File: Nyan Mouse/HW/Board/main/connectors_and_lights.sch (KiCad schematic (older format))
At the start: 49 parts, among them Q301 MOSFET-NCHANNELSMD, Q302 MOSFET-NCHANNELSMD, Q303 MOSFET-PCHANNELSMD, Q304 MOSFET-NCHANNELSMD, Q305 MOSFET-PCHANNELSMD, Q306 MOSFET-NCHANNELSMD, Q307 MOSFET-PCHANNELSMD, Q308 MOSFET-NCHANNELSMD, Q309 MOSFET-NCHANNELSMD, Q310 MOSFET-NCHANNELSMD, Q311 MOSFET-NCHANNELSMD, Q312 MOSFET-NCHANNELSMD, U301 74HC595, U302 74HC595, U303 74HC595

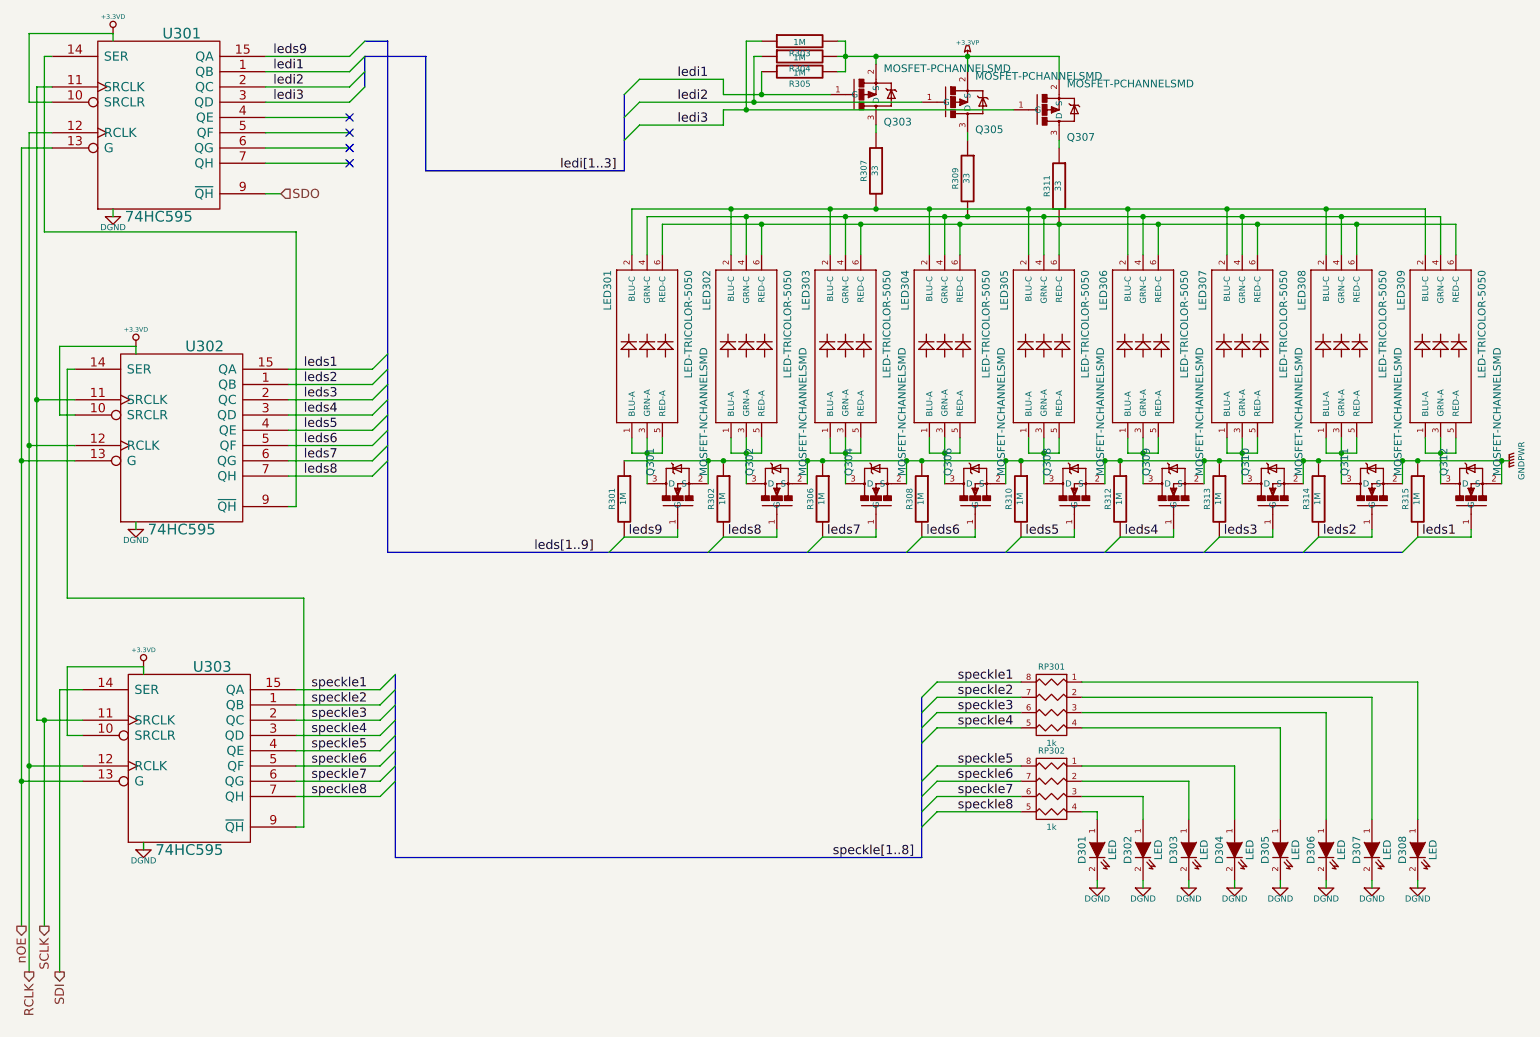
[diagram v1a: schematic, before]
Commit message: Flipped some RGB leds, added emitter pulldowns
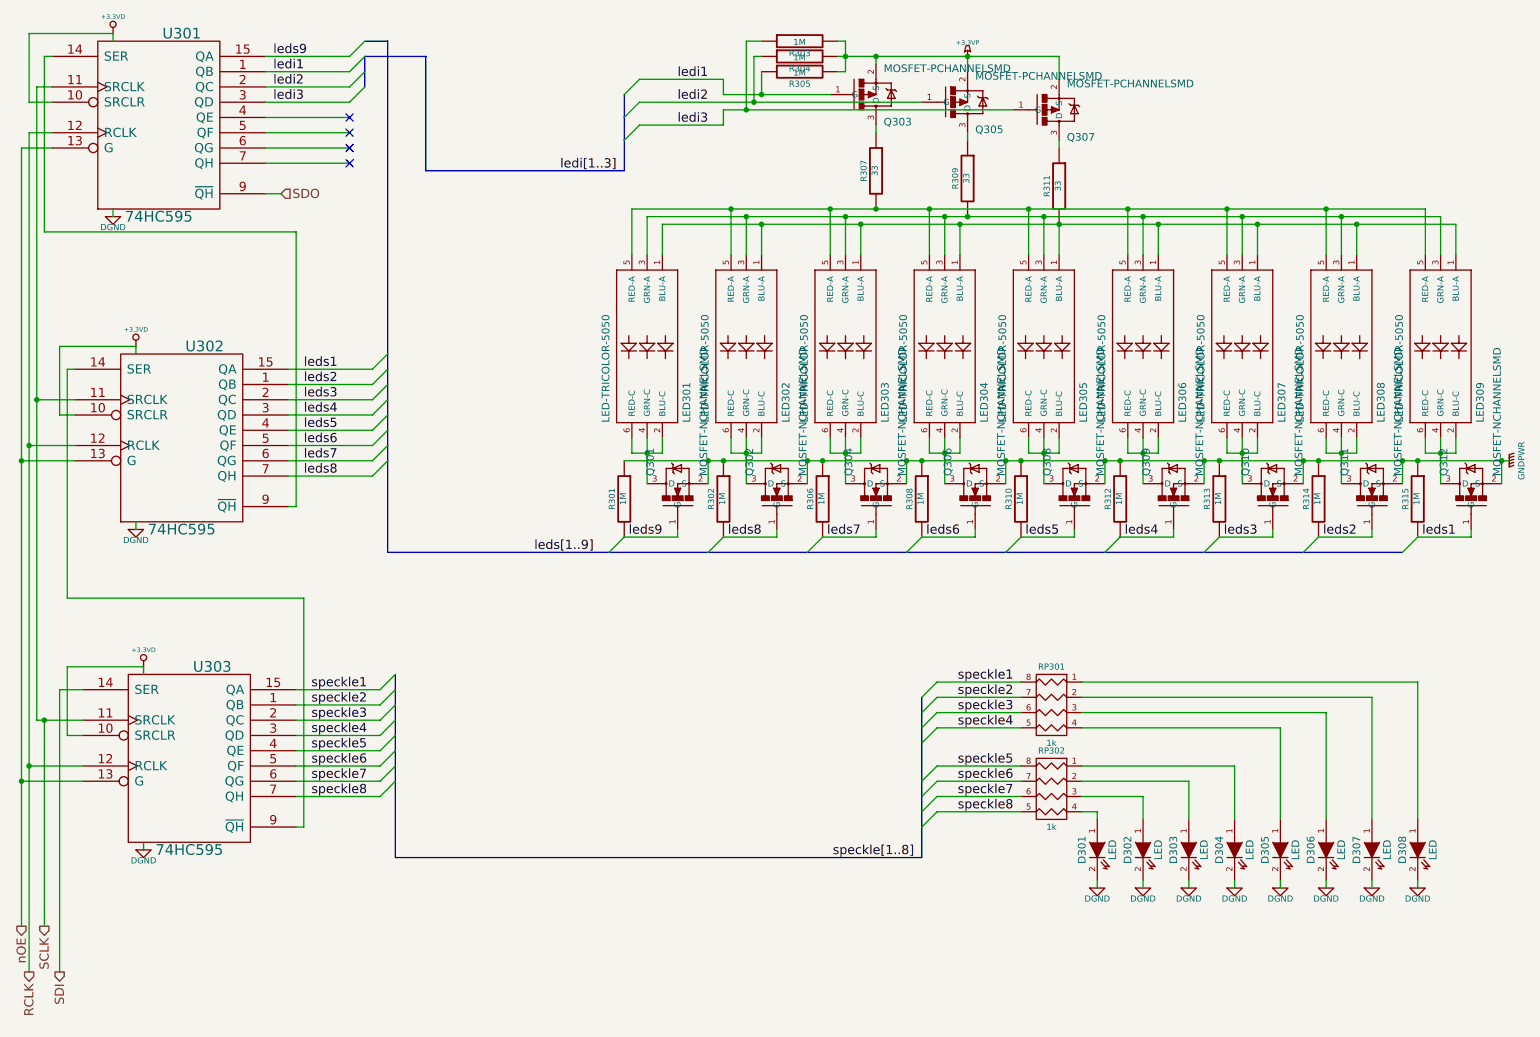
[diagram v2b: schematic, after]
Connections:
- new net: LED301.1 (BLU-A), LED302.1 (BLU-A), LED303.1 (BLU-A), LED304.1 (BLU-A), LED305.1 (BLU-A), LED306.1 (BLU-A), LED307.1 (BLU-A), LED308.1 (BLU-A), LED309.1 (BLU-A), R311.2
- new net: LED301.2 (BLU-C), LED301.4 (GRN-C), LED301.6 (RED-C), Q301.3 (D)
- new net: LED301.3 (GRN-A), LED302.3 (GRN-A), LED303.3 (GRN-A), LED304.3 (GRN-A), LED305.3 (GRN-A), LED306.3 (GRN-A), LED307.3 (GRN-A), LED308.3 (GRN-A), LED309.3 (GRN-A), R309.2
- new net: LED301.5 (RED-A), LED302.5 (RED-A), LED303.5 (RED-A), LED304.5 (RED-A), LED305.5 (RED-A), LED306.5 (RED-A), LED307.5 (RED-A), LED308.5 (RED-A), LED309.5 (RED-A), R307.2
- new net: LED302.2 (BLU-C), LED302.4 (GRN-C), LED302.6 (RED-C), Q302.3 (D)
- new net: LED305.2 (BLU-C), LED305.4 (GRN-C), LED305.6 (RED-C), Q308.3 (D)
- new net: LED306.2 (BLU-C), LED306.4 (GRN-C), LED306.6 (RED-C), Q309.3 (D)
- new net: LED307.2 (BLU-C), LED307.4 (GRN-C), LED307.6 (RED-C), Q310.3 (D)
- new net: LED308.2 (BLU-C), LED308.4 (GRN-C), LED308.6 (RED-C), Q311.3 (D)
- new net: LED309.2 (BLU-C), LED309.4 (GRN-C), LED309.6 (RED-C), Q312.3 (D)
- new net: LED303.2 (BLU-C), LED303.4 (GRN-C), LED303.6 (RED-C), Q304.3 (D)
- new net: LED304.2 (BLU-C), LED304.4 (GRN-C), LED304.6 (RED-C), Q306.3 (D)
